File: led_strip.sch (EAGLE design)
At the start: 18 parts, among them IC1 REG1117, IC2 MEGA8-AI, U1 MIC9.7MM, Y1 16MHz

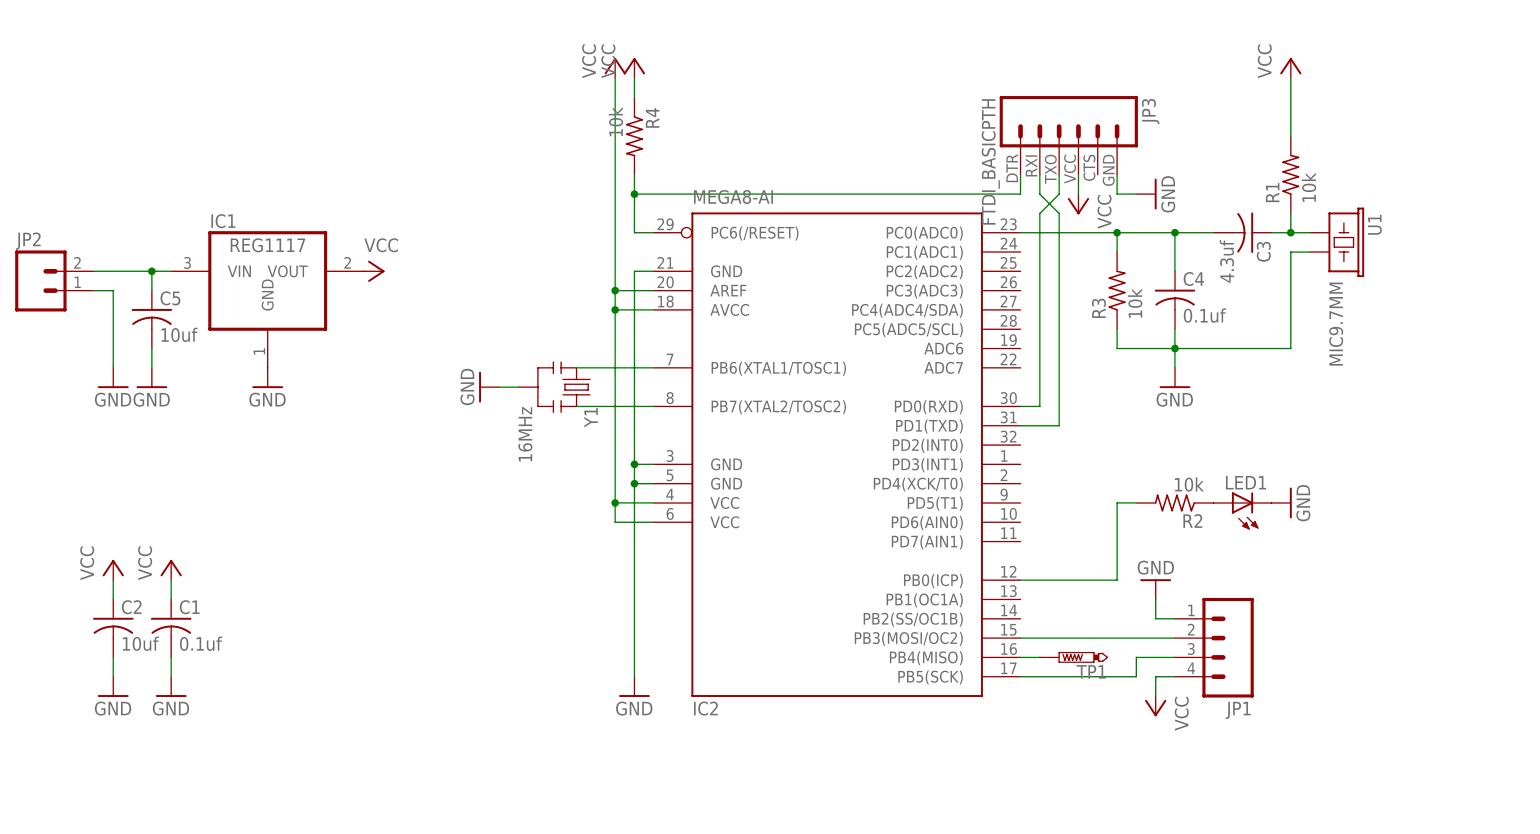
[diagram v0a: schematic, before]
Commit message: Added DTR capacitor for programming, reversed SPI header for LED stip.
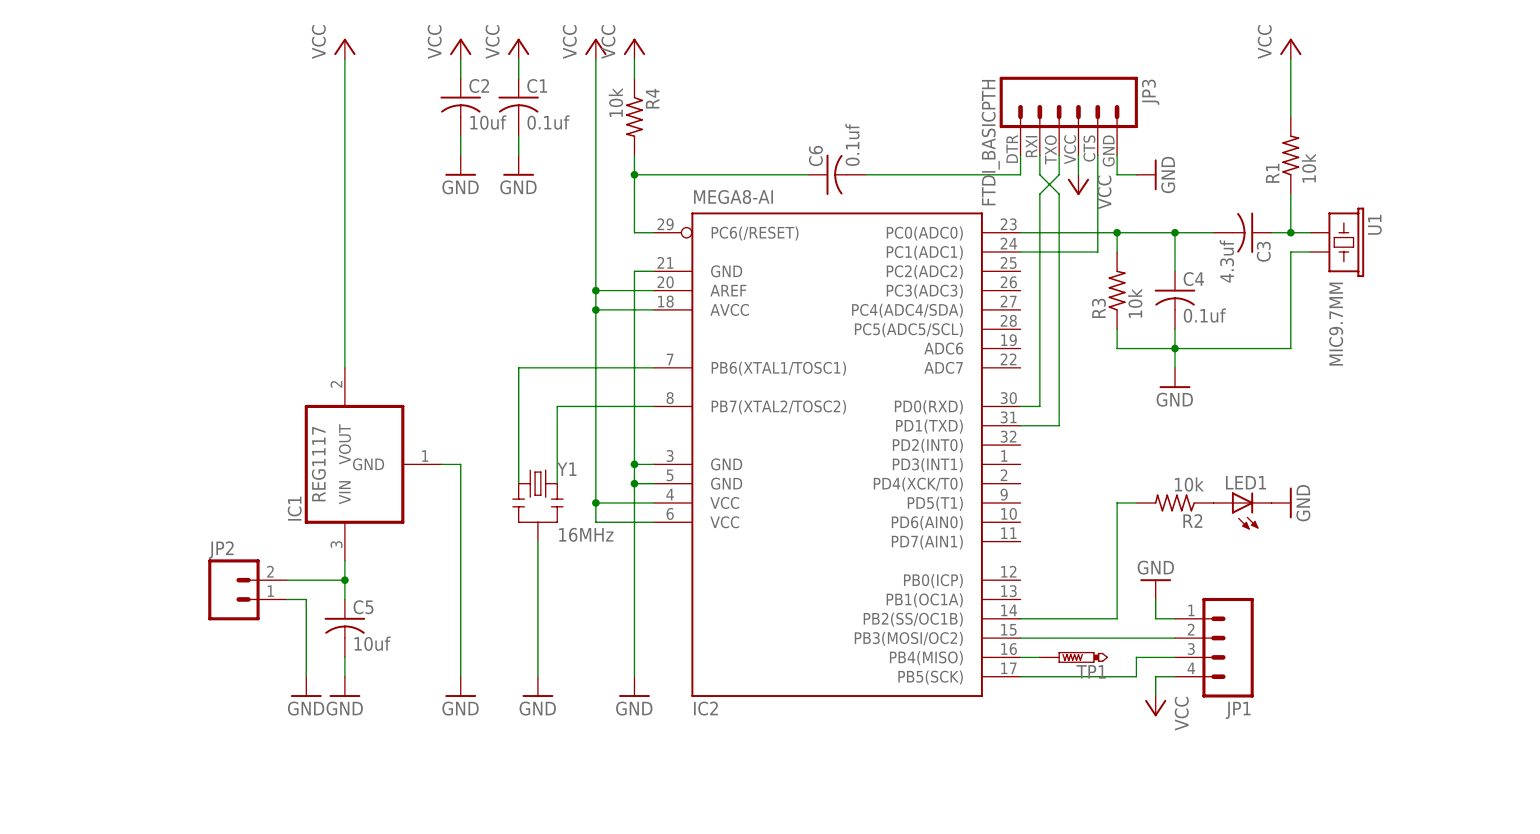
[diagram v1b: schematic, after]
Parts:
- added C6: 0.1uf, adafruit:C-USC1206
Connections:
- new net N$11: C6.2, JP3.1
- new net N$12: IC2.PC1(ADC1), JP3.5
- net N$18: now also IC2.PB2(SS/OC1B); no longer IC2.PB0(ICP)
- net N$7: now also C6.1; no longer JP3.1
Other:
- moved on the sheet: C1, C2, C5, IC1, JP2, JP3, R1, R4, Y1

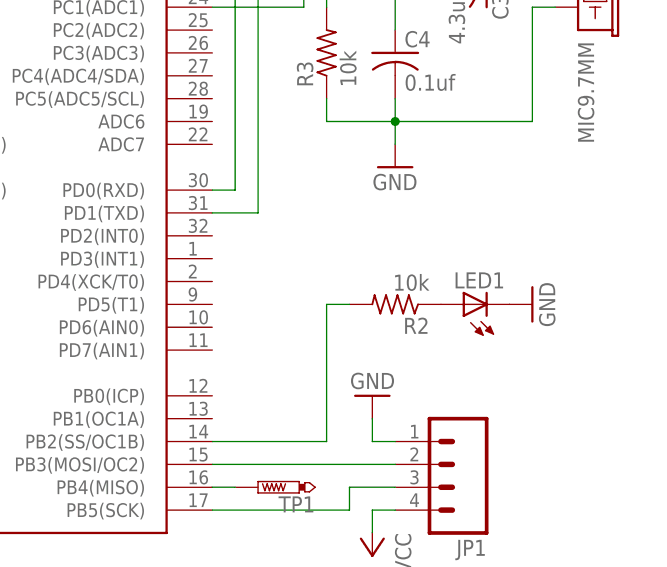
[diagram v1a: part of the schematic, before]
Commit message: Updated BOM, fixed LED current limiting resistor to sane value.
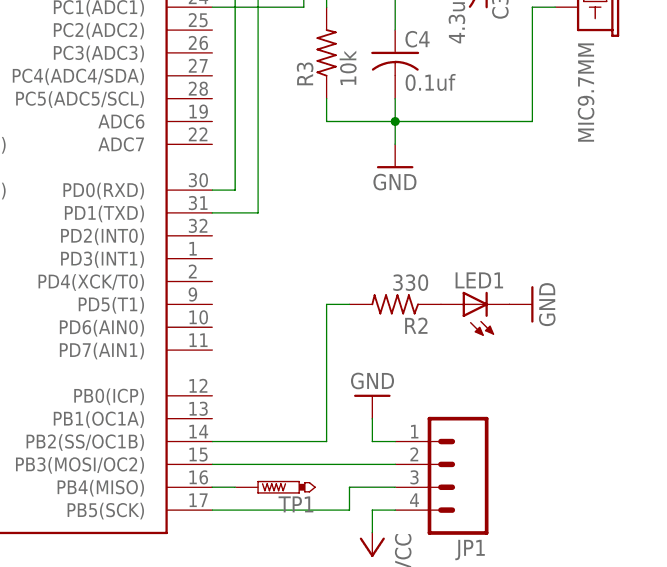
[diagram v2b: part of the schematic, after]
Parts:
- R2: value 10k -> 330
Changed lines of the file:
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@@
 <part name="LED1" library="adafruit" deviceset="LED" device="CHIPLED_1206"/>
 <part name="GND2" library="sparkfun" deviceset="GND" device=""/>
-<part name="R2" library="adafruit" deviceset="R-US_" device="R1206" value="10k"/>
+<part name="R2" library="adafruit" deviceset="R-US_" device="R1206" value="330"/>
 <part name="GND19" library="sparkfun" deviceset="GND" device=""/>
 <part name="IC1" library="burr-brown" deviceset="REG1117" device=""/>

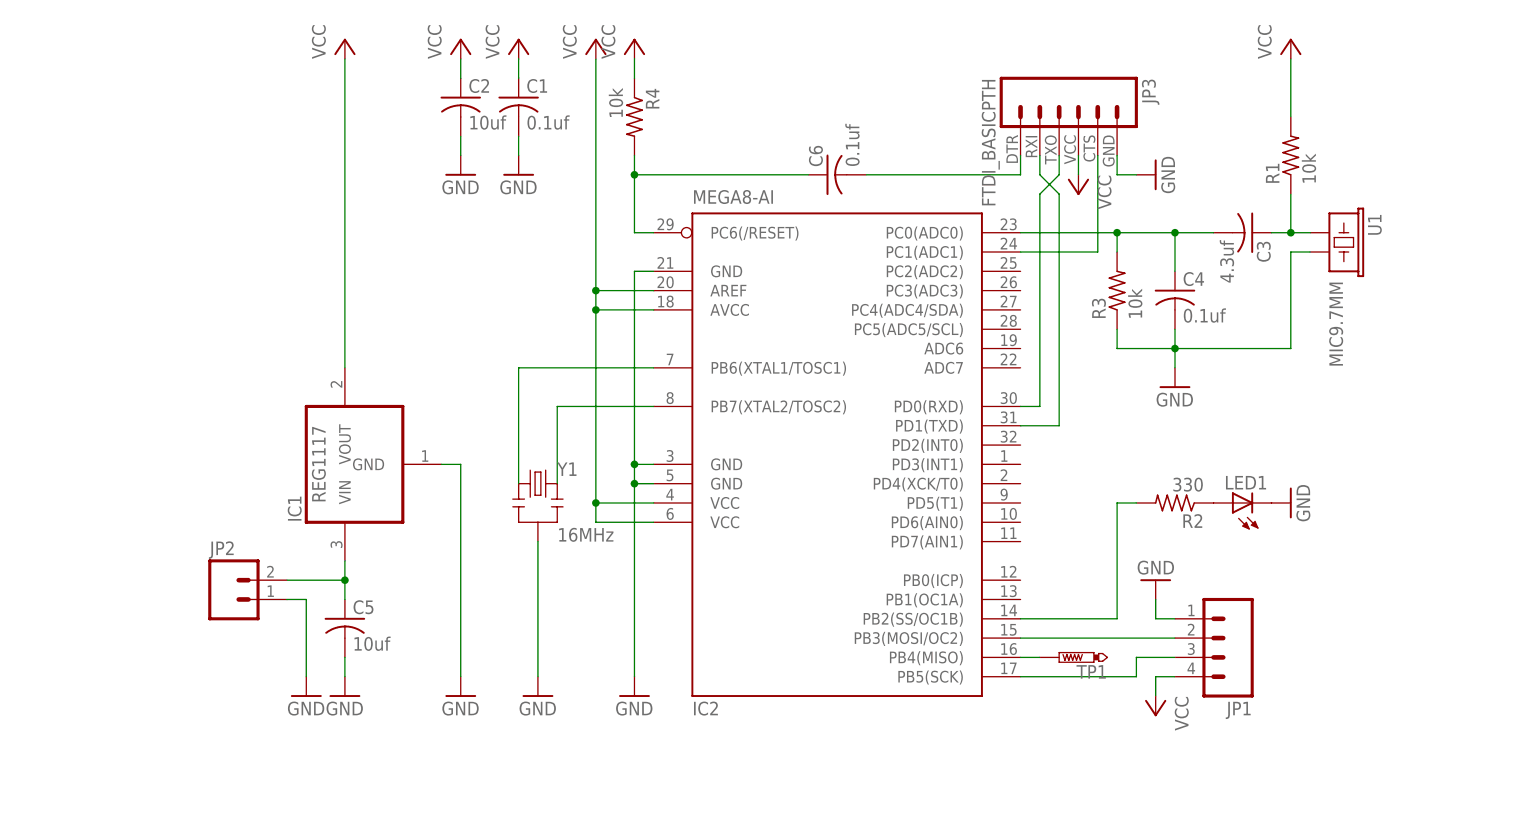
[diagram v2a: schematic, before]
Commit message: Created usb bootloader varient.
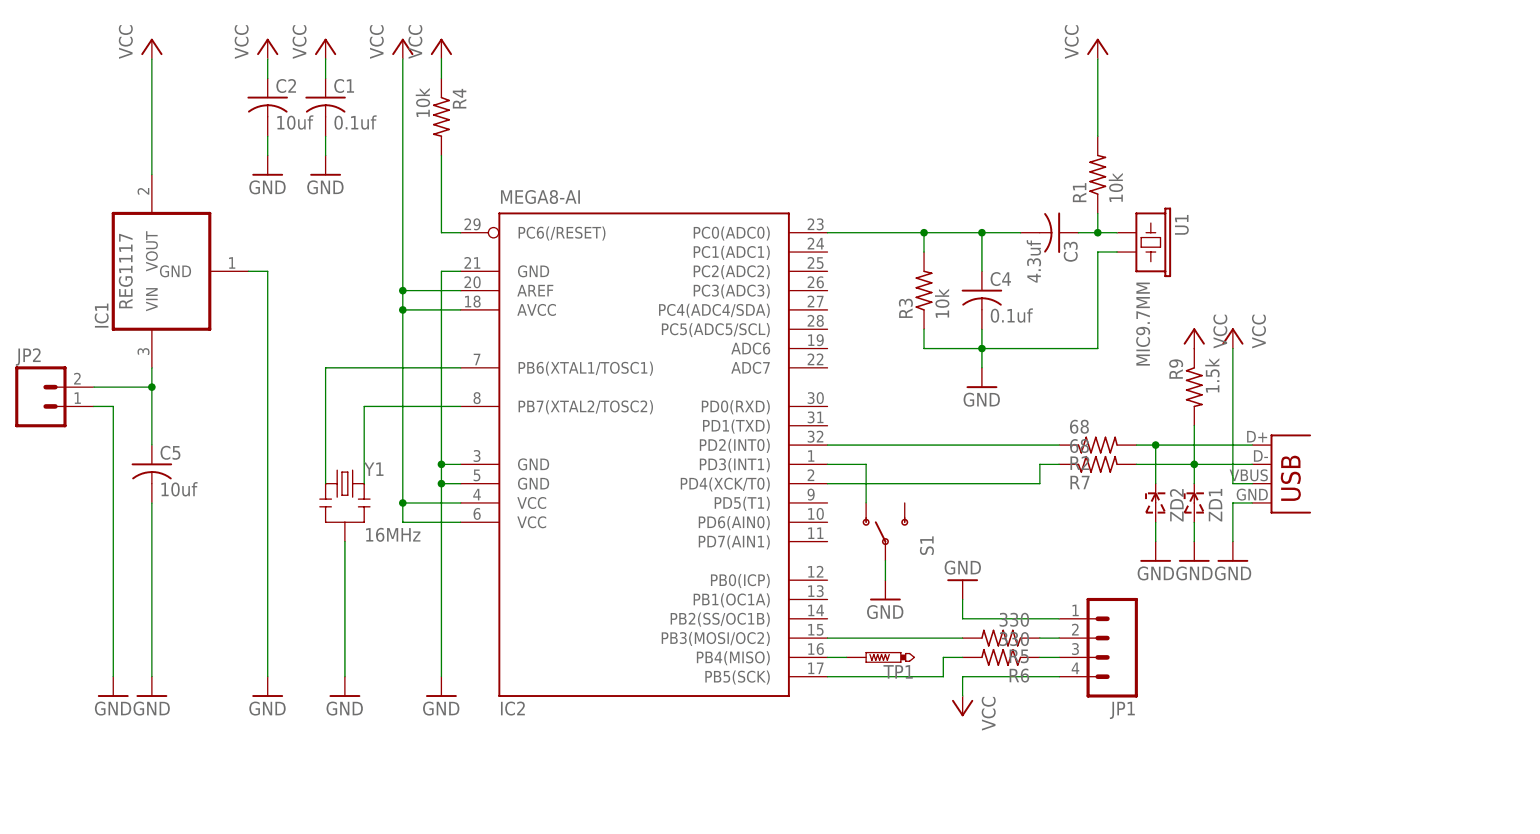
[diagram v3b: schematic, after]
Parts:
- removed C6: 0.1uf, adafruit:C-USC1206
- removed JP3: FTDI_BASICPTH, sparkfun:FTDI_BASICPTH
- removed LED1: (no value), adafruit:LEDCHIPLED_1206
- added R5, R6: 330, adafruit:R-US_R0805
- added R7: 68, adafruit:R-US_R0805
- added R9: 1.5k, adafruit:R-US_R0805
- added S1: (no value), sparkfun:SWITCH-SPSTSMD2
- added X1: USB-SMD-NS, sparkfun:USB-SMD-NS
- added ZD1, ZD2: (no value), dp_devices:ZENERSOD-323F
- C1, C2, C3, C4, C5: device adafruit:C-USC1206 -> adafruit:C-USC0805
- R1, R3, R4: device adafruit:R-US_R1206 -> adafruit:R-US_R0805
- R2: value 330 -> 68; device adafruit:R-US_R1206 -> adafruit:R-US_R0805
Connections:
- removed net N$18: IC2.PB2(SS/OC1B), R2.2
- new net N$14: JP1.3, R6.1
- new net N$15: IC2.PB3(MOSI/OC2), R5.2
- net GND: now also S1.P, X1.GND, ZD1.A, ZD2.A; no longer JP3.6, LED1.C
- net N$1: now also R6.2; no longer JP1.3
- net N$11: now also IC2.PD4(XCK/T0), R7.1; no longer C6.2, JP3.1
- net N$12: now also IC2.PD2(INT0), R2.1; no longer IC2.PC1(ADC1), JP3.5
- net N$13: now also IC2.PD3(INT1), S1.O; no longer LED1.A, R2.1
- net N$3: now also R5.1; no longer IC2.PB3(MOSI/OC2)
- net N$4: now also R2.2, X1.D+, ZD2.C; no longer IC2.PD0(RXD), JP3.3
- net N$5: now also R7.2, R9.2, X1.D-, ZD1.C; no longer IC2.PD1(TXD), JP3.2
- net N$7: no longer C6.1
- net VCC: now also R9.1, X1.VBUS; no longer JP3.4
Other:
- moved on the sheet: C1, C2, C3, C4, C5, IC1, IC2, JP1, JP2, R1, R2, R3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

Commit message: Fixed up layout for ordering.
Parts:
- removed R9: 1.5k, adafruit:R-US_R0805
- added R8: 10k, adafruit:R-US_R0805
- added RST: PTR1B1,27, testpad:PTR1B1,27
- C4: value 0.1uf -> 10uf
- C5: value 10uf -> 0.1uf
- R2: value 68 -> 330
- R3: value 10k -> 1.5k
- R6: value 330 -> 68
- renumbered TP1 to MISO
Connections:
- net GND: now also R4.1; no longer R3.1
- net N$1: now also R2.2; no longer R6.2
- net N$11: now also R6.1; no longer R7.1
- net N$12: now also R7.1; no longer R2.1
- net N$14: now also R2.1; no longer R6.1
- net N$20: now also C4.1; no longer C5.1
- net N$4: now also R7.2; no longer R2.2
- net N$5: now also R3.2, R6.2; no longer R7.2, R9.2
- net N$7: now also R8.2, RST.TP; no longer R4.2
- net N$9: now also C5.1, R4.2; no longer C4.1, R3.2
- net VCC: now also R3.1, R8.1; no longer R4.1, R9.1
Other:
- moved on the sheet: C4, C5, R2, R3, R4, R6, R7

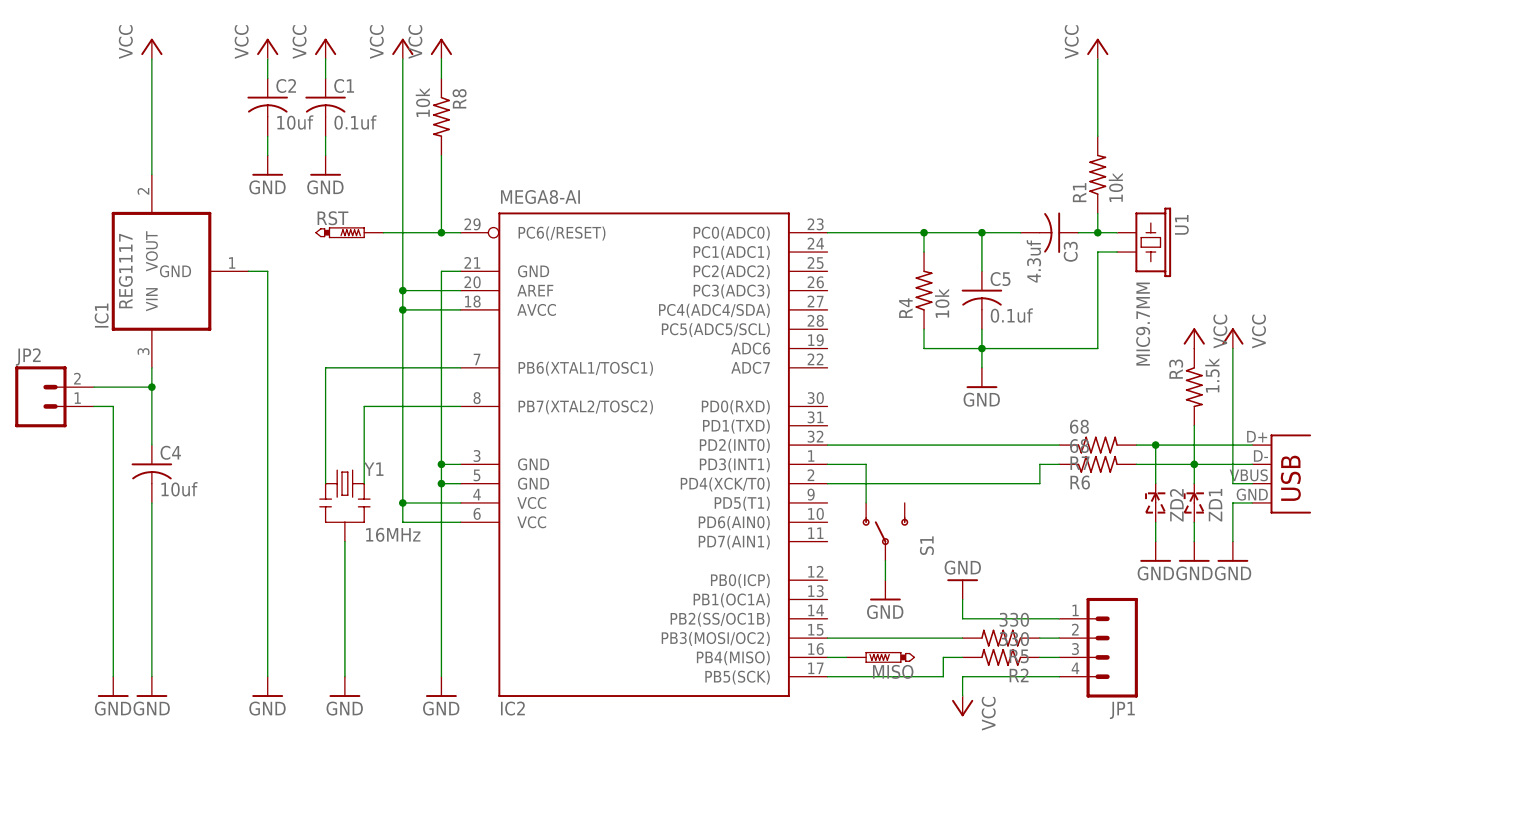
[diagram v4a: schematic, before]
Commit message: still adding io pins, fixed mic input issue
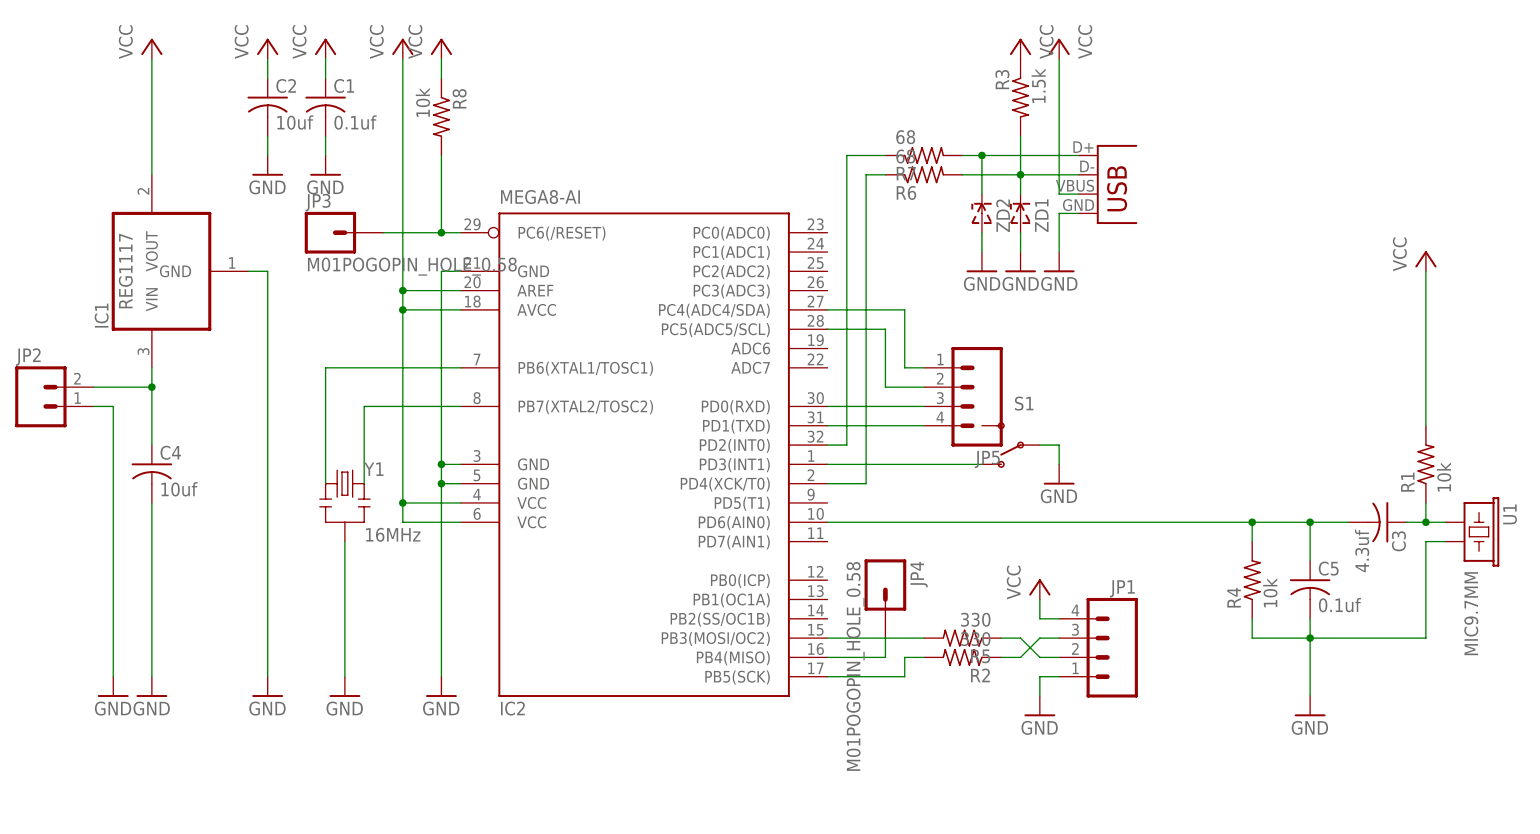
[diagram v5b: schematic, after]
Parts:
- removed MISO, RST: PTR1B1,27, testpad:PTR1B1,27
- added JP3, JP4: M01POGOPIN_HOLE_0.58, sparkfun:M01POGOPIN_HOLE_0.58
- added JP5: (no value), sparkfun:M04PTH
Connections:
- new net N$16: IC2.PD0(RXD), JP5.3
- new net N$17: IC2.PD1(TXD), JP5.4
- new net N$18: IC2.PC5(ADC5/SCL), JP5.2
- new net N$19: IC2.PC4(ADC4/SDA), JP5.1
- net N$2: now also JP4.1; no longer MISO.TP
- net N$7: now also JP3.1; no longer RST.TP
- net N$9: now also IC2.PD6(AIN0); no longer IC2.PC0(ADC0)
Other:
- moved on the sheet: C3, C5, JP1, R1, R2, R3, R4, R5, R6, R7, S1, U1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
